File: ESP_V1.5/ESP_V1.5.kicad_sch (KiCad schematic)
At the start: 195 parts

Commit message: Quick Cleanup
Added ToDo's, not much else need sleep
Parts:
- removed U?: ~, symbol Imported_Symbols:TL2575HV-05QKTTRQ1
- C? (x3): value (none) -> 0.1u
- C? (x2): value (none) -> 3.3n
- C? (x4): value (none) -> 1u
- C? (x10): value (none) -> 10u
- C? (x10): value (none) -> 100n
- C? (x2): value (none) -> 0.47uF
- C? (x2): value (none) -> 10n
- C?: value (none) -> 22u
- C?: value (none) -> C
- C? (x2): value (none) -> 22pF; footprint (none) -> Capacitor_SMD:C_0402_1005Metric
- C?: value (none) -> 4.7u
- IC?: value (none) -> W25Q128JVSIQ; footprint (none) -> SOIC127P790X216-8N
- IC?: value (none) -> TPS54226PWPR; footprint (none) -> SOP65P640X120-15N
- IC?: value (none) -> RP2040; footprint (none) -> QFN40P700X700X90-57N-D
- IC?: value (none) -> MCP1790T-5002E_DB; footprint (none) -> SOT230P700X180-4N
- J?: value (none) -> USB_C_Receptacle_USB2.0
- J? (x5): value (none) -> 1985807; footprint (none) -> 1985807
- Q? (x8): value (none) -> MBT2222ADW1T1; footprint (none) -> Package_TO_SOT_SMD:SOT-363_SC-70-6
- Q? (x4): value (none) -> BSS138; footprint (none) -> Package_TO_SOT_SMD:SOT-23
- R? (x13): value (none) -> 10k
- R?: value (none) -> 0.1
- R? (x2): value (none) -> 5.1k
- R? (x3): value (none) -> R_US
- R?: value (none) -> 10
- R? (x2): value (none) -> 27
- R?: value (none) -> 100
- R? (x2): value (none) -> 200k
- R? (x2): value (none) -> 1k
- R? (x2): value (none) -> R
- R? (x3): value (none) -> 100k
- R? (x2): value (none) -> 20k
- R? (x2): value (none) -> 150
- R?: value (none) -> 22.1k
- R?: value (none) -> 0.01
- R?: value (none) -> 73.2k
- R? (x2): value (none) -> 680
- SW?: value (none) -> SW_MEC_5E
- SW? (x2): value (none) -> SW_SPST
- TH? (x2): value (none) -> NTGC103JX
- U?: value (none) -> KMR231NGLFS; footprint (none) -> IC4_KMR231NGLFS_CNK
- U? (x4): value (none) -> 1043; footprint (none) -> 1043_KEY
- U? (x2): value (none) -> IRF7503TRPBF; footprint (none) -> IRF7503TRPBF_INF
- U?: value (none) -> MAX706RESA+; footprint (none) -> 21-0041B_8_MXM
- U? (x2): value (none) -> BQ29702; footprint (none) -> Package_SON:WSON-6_1.5x1.5mm_P0.5mm
- U?: value (none) -> ADM1176-1ARMZ-R7; footprint (none) -> RM_10_ADI
- U?: value (none) -> MAX17205G+T; footprint (none) -> 21-0137_T1433-2C_MXM
- Y?: value (none) -> 12MHz; footprint (none) -> Crystal:Crystal_SMD_3225-4Pin_3.2x2.5mm
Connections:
- net GND: now also TH?.2, TH?.2
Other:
- note added: "To Do's: 1.Verify Net connections between A's and C's circuits 2.Add 5v Switching Regulator @ Heater - Austin 3.Breakout pins for power and ground debugging 4.40 pin backplane connector 5.add footprint libraries to this folder"

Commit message: Added 5V Reg and Heater
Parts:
- added C?: (no value), symbol Device:C
- added C?: 47uF, symbol Device:C
- added D?: 1N5821, Diode_THT:D_DO-201AD_P15.24mm_Horizontal, symbol Diode:1N5821
- added J?: (no value), symbol Connector_Generic:Conn_01x02
- added L?: (no value), symbol Imported_Symbols:DO3316P-103MLD
- added R?: (no value), symbol Device:R
- added U?: (no value), symbol Imported_Symbols:TL2575HV-05QKTTRQ1
- added U?: IRF7503TRPBF, IRF7503TRPBF_INF, symbol Imported_Symbols:IRF7503TRPBF
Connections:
- net +5V: now also C?.1, D?.1 (K), J?.1 (Pin_1), L?.2, R?.1
- net GND: now also C?.2, C?.2, D?.2 (A), U?.1 (S1), U?.3 (GND), U?.6 (EPAD)
- net VBat_Pos: now also C?.1, U?.1 (VIN)
- net 3.3V: now reaches J?.6 (Pin_6)
- new net: L?.1, U?.2 (OUTPUT)
- new net: R?.2, U?.4 (FEEDBACK)
- new net: J?.2 (Pin_2), U?.8 (D1)
- new net 5V_En: U?.5 (*ON/OFF)
- new net HEAT_En: U?.2 (G1)
- no-connect marks 9 -> 8
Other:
- note added: "49ohm heater resistance 6v/49=122mA -> 0.7W Using HK6903"
- note added: "5V Switching Regulator 1A output"
- note added: "Heater Connector"

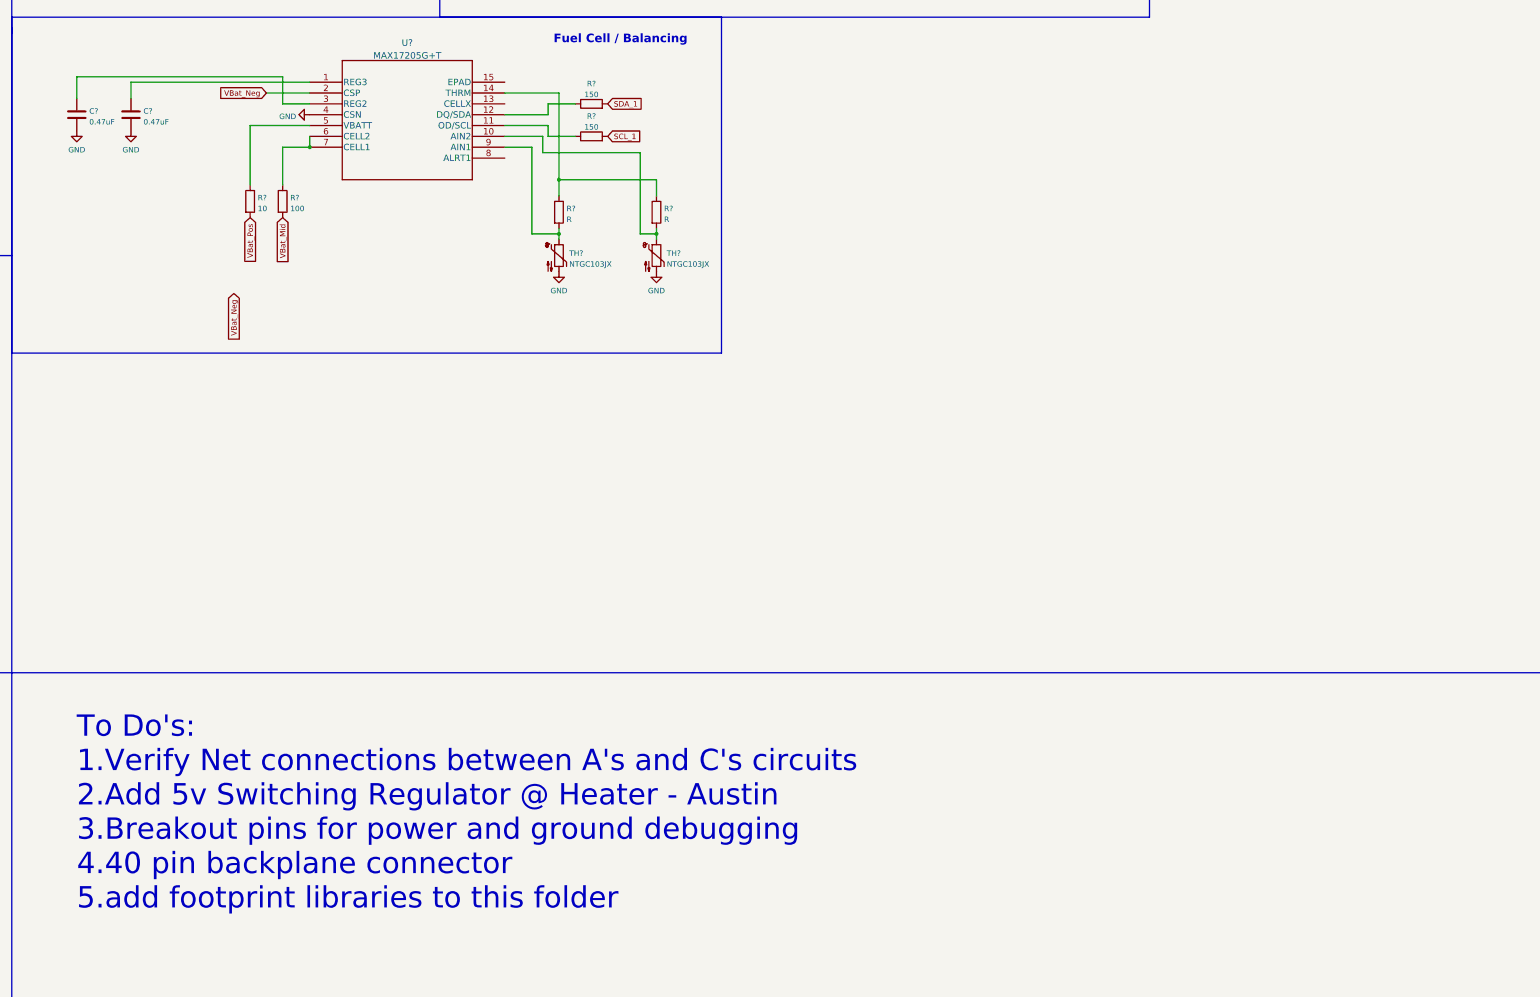
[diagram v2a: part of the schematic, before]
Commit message: Edited ToDo's
99% of features are now implemented, need to clean up nets and add footprints for MPPT IC's.

Then ready for layout!
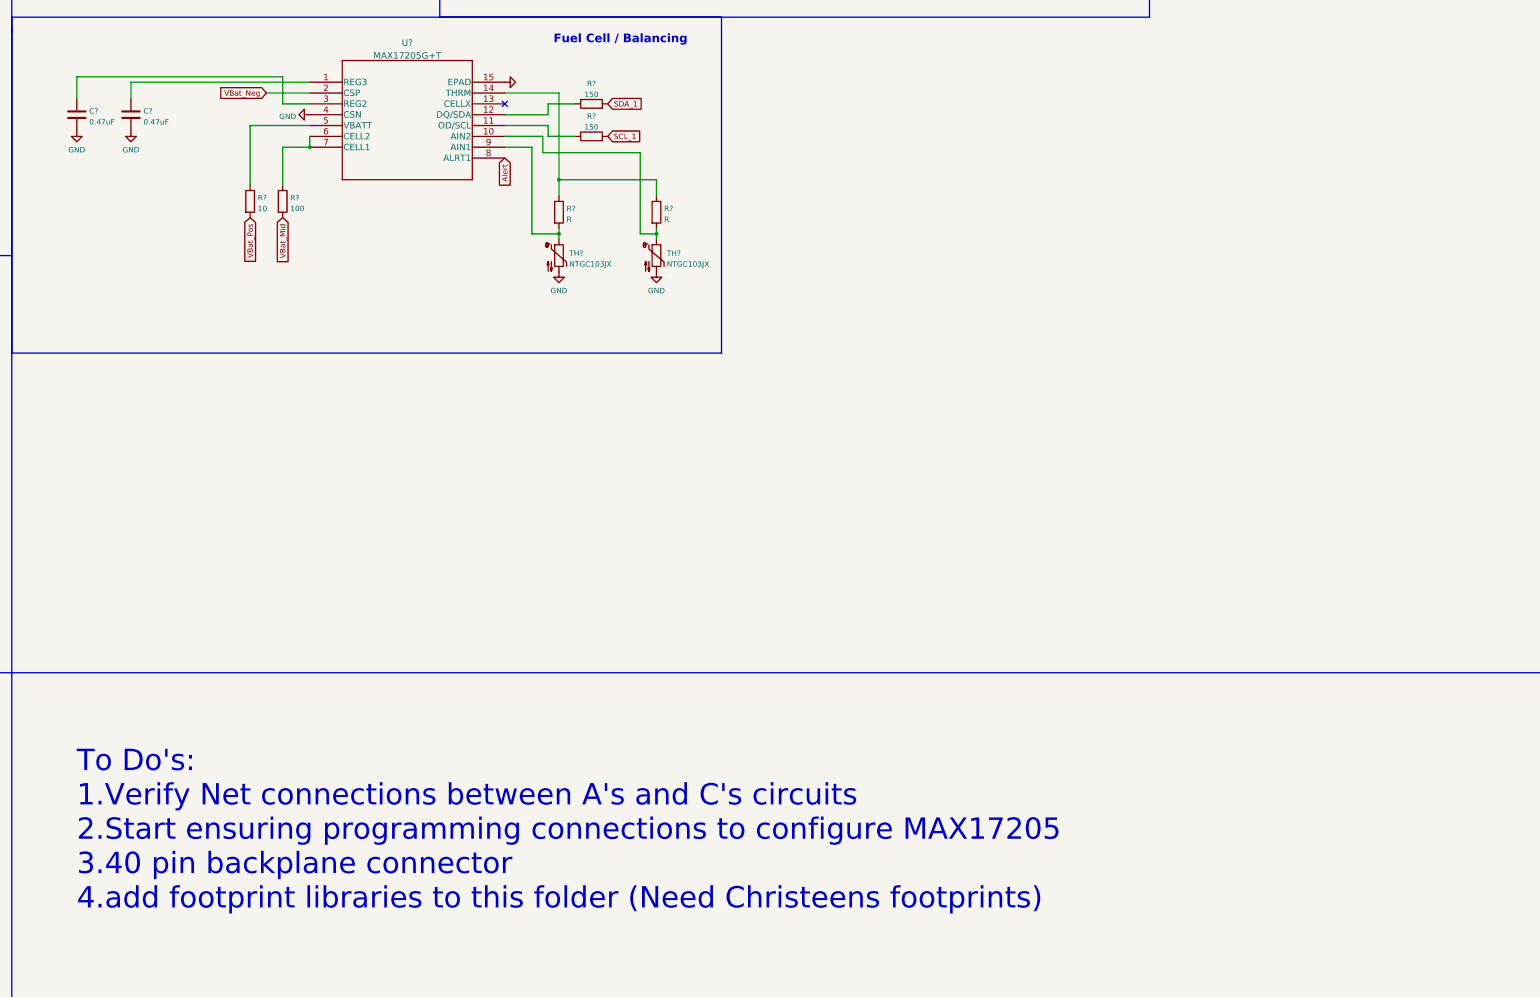
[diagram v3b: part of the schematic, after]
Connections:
- net GND: now also U?.15 (EPAD)
- net Alert: now reaches U?.8 (ALRT1)
- no-connect marks 8 -> 9
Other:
- note added: "To Do's: 1.Verify Net connections between A's and C's circuits 2.Start ensuring programming connections to configure MAX17205 3.40 pin backplane connector 4.add footprint libraries to this folder (Need Christeens footprints)"
- note removed: "To Do's: 1.Verify Net connections between A's and C's circuits 2.Add 5v Switching Regulator @ Heater - Austin 3.Breakout pins for power and ground debugging 4.40 pin backplane connector 5.add footprint libraries to this folder"
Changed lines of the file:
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@@
   (no_connect (at 209.55 167.64))
   (no_connect (at 631.19 125.73))
+  (no_connect (at 501.65 161.29))
   (no_connect (at 347.98 34.29))
   (no_connect (at 631.19 120.65))
@@
     (effects (font (size 1.27 1.27)) (justify left bottom))
   )
-  (text "To Do's:\n1.Verify Net connections between A's and C's circuits\n2.Add 5v Switching Regulator @ Heater - Austin\n3.Breakout pins for power and ground debugging\n4.40 pin backplane connector\n5.add footprint libraries to this folder"
+  (text "To Do's:\n1.Verify Net connections between A's and C's circuits\n2.Start ensuring programming connections to configure MAX17205\n3.40 pin backplane connector\n4.add footprint libraries to this folder (Need Christeens footprints)"
     (at 401.32 350.52 0)
     (effects (font (size 5 5)) (justify left bottom))
@@
     )
   )
-  (global_label "VBat_Neg" (shape input) (at 438.15 205.74 270) (fields_autoplaced)
+  (global_label "Alert" (shape input) (at 501.65 173.99 270) (fields_autoplaced)
     (effects (font (size 1.27 1.27)) (justify right))
-    (property "Intersheet References" "${INTERSHEET_REFS}" (id 0) (at 438.0706 216.9221 90)
+    (property "Intersheet References" "${INTERSHEET_REFS}" (id 0) (at 501.5706 180.7574 90)
       (effects (font (size 1.27 1.27)) (justify right) hide)
     )
@@
     (pin "1")
   )
+  (symbol (lib_id "power:GND") (at 501.65 156.21 90) (unit 1)
+    (in_bom yes) (on_board yes) (fields_autoplaced)
+    (property "Reference" "#PWR?" (id 0) (at 508 156.21 0)
+      (effects (font (size 1.27 1.27)) hide)
+    )
+    (property "Value" "" (id 1) (at 504.825 156.6438 90)
+      (effects (font (size 1.27 1.27)) (justify right))
+    )
+    (property "Footprint" "" (id 2) (at 501.65 156.21 0)
+      (effects (font (size 1.27 1.27)) hide)
+    )
+    (property "Datasheet" "" (id 3) (at 501.65 156.21 0)
+      (effects (font (size 1.27 1.27)) hide)
+    )
+    (pin "1")
+  )
   (symbol (lib_id "Device:C") (at 280.67 274.32 0) (unit 1)
     (in_bom yes) (on_board yes) (fields_autoplaced)
@@
       (reference "#PWR?") (unit 1) (value "GND") (footprint "")
     )
+    (path "/d0cb2b73-1fc3-4829-9c94-3ea1c54d65dc"
+      (reference "#PWR?") (unit 1) (value "GND") (footprint "")
+    )
